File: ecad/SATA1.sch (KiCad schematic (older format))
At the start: 57 parts, among them IC14 TUSB9261IPVP, IC15 IS25LQ010B, J16 Conn_SATA, Y5 40MHz

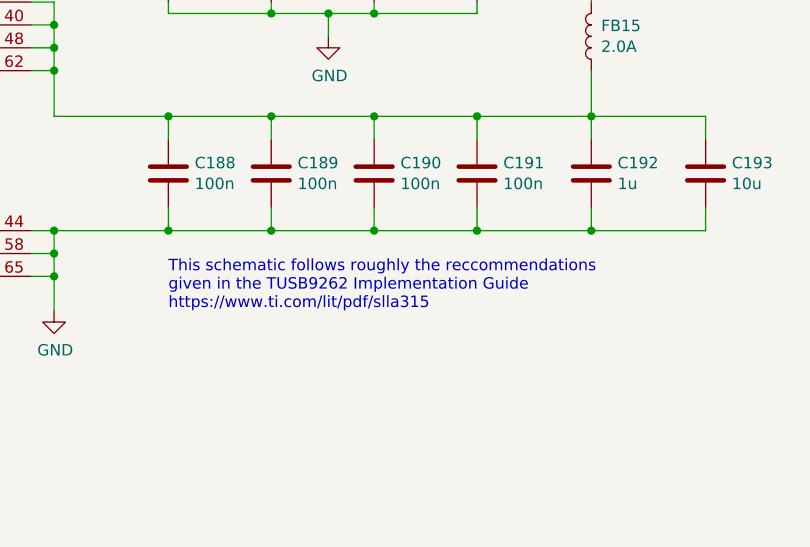
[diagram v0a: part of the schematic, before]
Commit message: Fixing Schematic Annotation
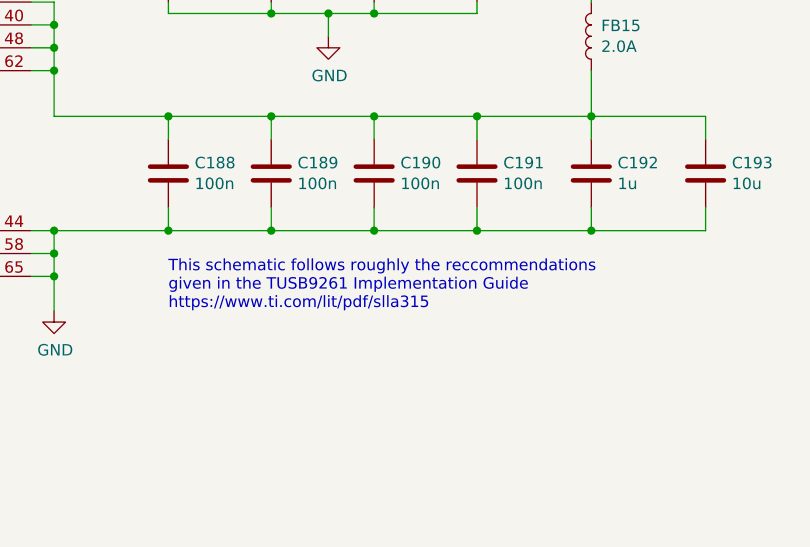
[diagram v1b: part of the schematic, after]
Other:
- note added: "This schematic follows roughly the reccommendations \ngiven in the TUSB9261 Implementation Guide\nhttps://www.ti.com/lit/pdf/slla315"
- note removed: "This schematic follows roughly the reccommendations \ngiven in the TUSB9262 Implementation Guide\nhttps://www.ti.com/lit/pdf/slla315"
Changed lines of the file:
@@
 	8750 1500 9100 1500
 Text Notes 5650 6350 0    50   ~ 0
-This schematic follows roughly the reccommendations \ngiven in the TUSB9262 Implementation Guide\nhttps://www.ti.com/lit/pdf/slla315
+This schematic follows roughly the reccommendations \ngiven in the TUSB9261 Implementation Guide\nhttps://www.ti.com/lit/pdf/slla315
 $EndSCHEMATC
